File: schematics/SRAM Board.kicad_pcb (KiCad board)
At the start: 2 copper layers, 105.4 x 50.8 mm, 15 parts, among them U1 SN74ABT821ADW, U16 44256_DRAM, U17 44256_DRAM, U18 44256_DRAM, U19 44256_DRAM, U2 74HC00, U20 44256_DRAM, U21 44256_DRAM, U22 44256_DRAM, U23 44256_DRAM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

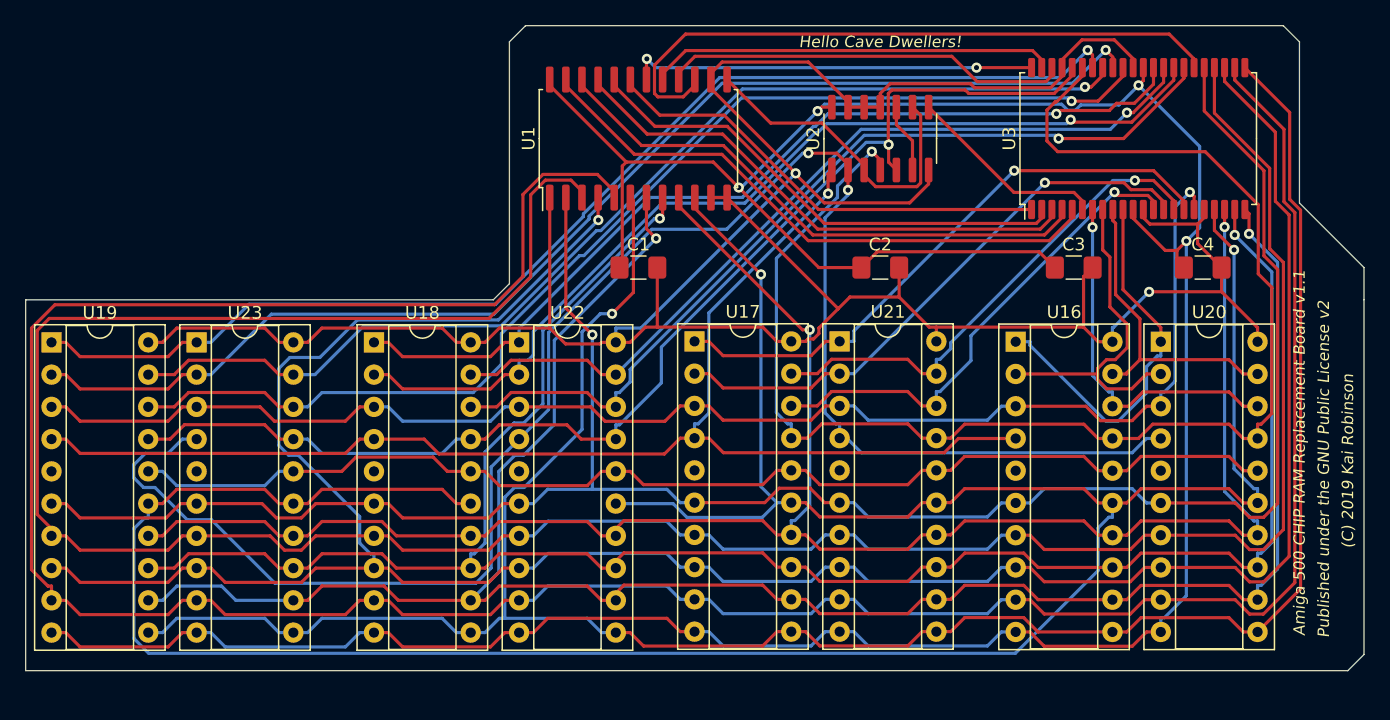
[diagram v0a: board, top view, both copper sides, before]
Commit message: Add files via upload
Fixing a glaring error - I had grounded A18, rather than assigning it to _bras0 instead.
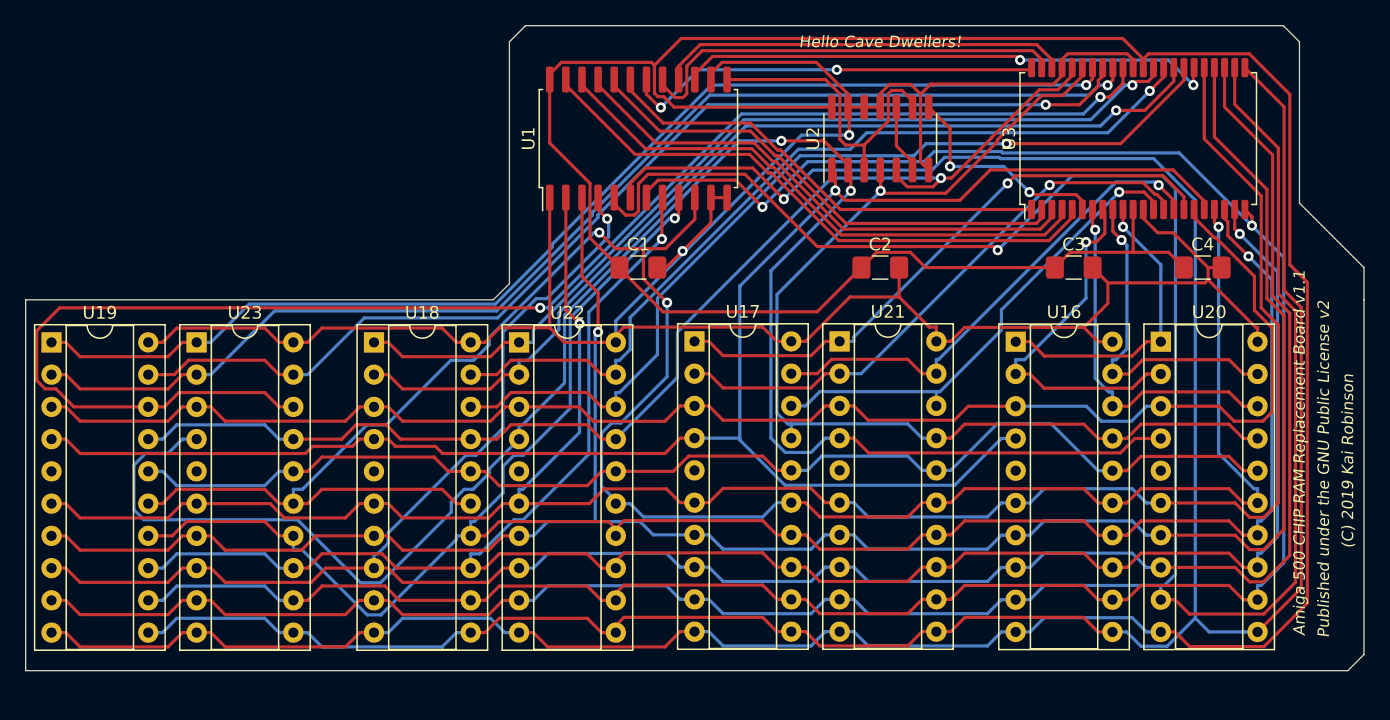
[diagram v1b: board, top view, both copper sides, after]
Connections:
- U3 pad 18: /gnd -> /_bras0
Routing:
- net /vcc5: track 241.9 -> 297.4 mm, vias 4 -> 0
- net /a8: track 229.3 -> 174.8 mm, vias 2 -> 3
- net /a4: track 180.0 -> 225.9 mm
- net /a1: track 212.6 -> 169.5 mm, vias 0 -> 1
- net /_bras0: track 104.6 -> 137.4 mm
- net /d12: track 90.8 -> 120.8 mm, vias 1 -> 2
- net /_lcas: track 112.8 -> 84.7 mm
- net /gnd: track 233.3 -> 211.8 mm
- net /a5: track 165.6 -> 181.1 mm
- net /a2: track 197.1 -> 184.2 mm
- net /ma8: track 51.4 -> 42.6 mm, vias 0 -> 2
- net /_we: track 113.4 -> 122.1 mm, vias 1 -> 0
- net /a7: track 153.3 -> 161.2 mm
- net /a3: track 226.4 -> 234.0 mm, vias 0 -> 1
- net /d3: track 30.3 -> 24.0 mm, vias 0 -> 1
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
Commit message: Add files via upload
Switching the 74ABT00 pin 11 from GND to NC
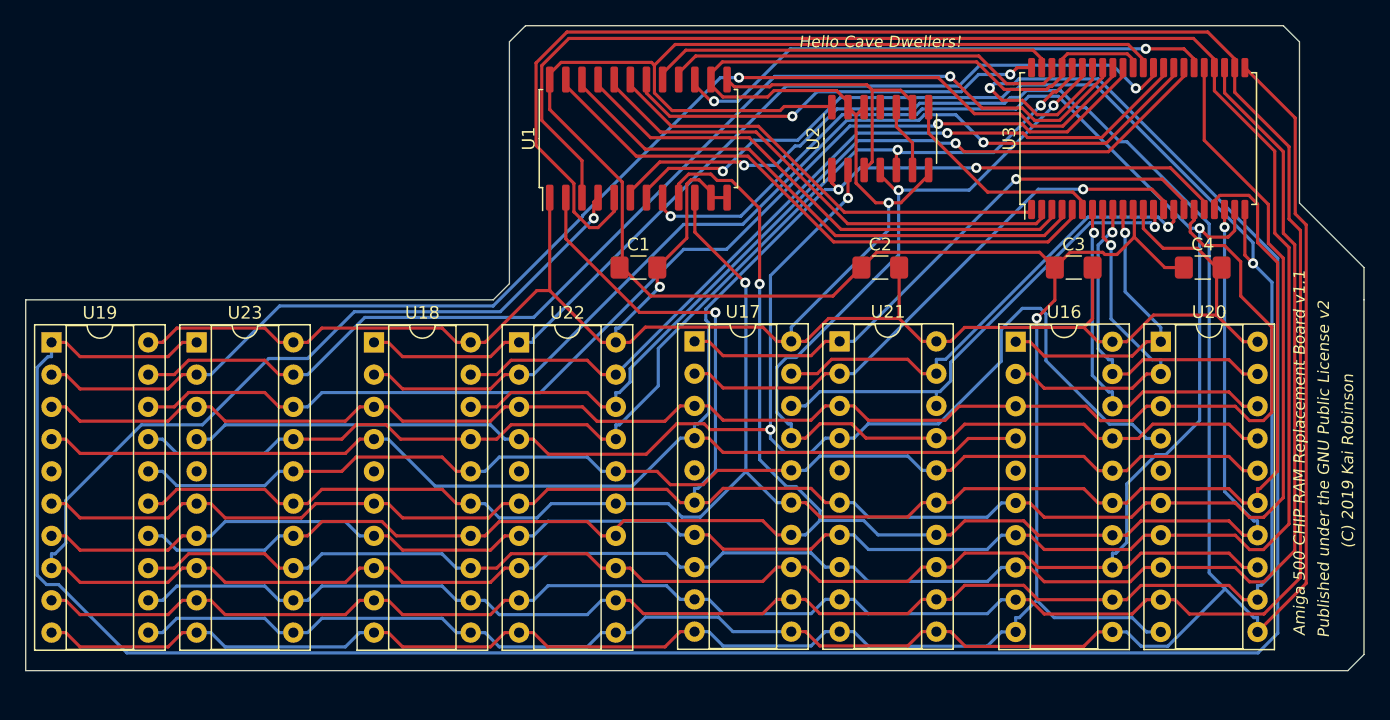
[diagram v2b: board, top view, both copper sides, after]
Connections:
- U2 pad 11: /gnd -> /nc
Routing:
- net /d15: track 92.5 -> 201.6 mm
- net /a1: track 169.5 -> 210.6 mm, vias 1 -> 0
- net /vcc5: track 297.4 -> 257.7 mm, vias 0 -> 1
- net /d12: track 120.8 -> 89.7 mm, vias 2 -> 1
- net /_bras1: track 144.4 -> 115.3 mm
- net /a8: track 174.8 -> 148.7 mm, vias 3 -> 1
- net /a2: track 184.2 -> 204.8 mm
- net /a6: track 161.2 -> 180.6 mm
- net /gnd: track 211.8 -> 225.3 mm
- net /a3: track 234.0 -> 224.7 mm, vias 1 -> 0
- net /a0: track 167.5 -> 174.4 mm
- net /a7: track 161.2 -> 157.3 mm
- net /a5: track 181.1 -> 184.9 mm
- net /d13: track 95.2 -> 98.2 mm
- net /a4: track 225.9 -> 228.7 mm
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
